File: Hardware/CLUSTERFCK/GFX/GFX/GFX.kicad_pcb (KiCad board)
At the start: 4 copper layers, 141.9 x 122.1 mm, 302 parts, among them J1 Conn_02x20_Counter_Clockwise, J2 Conn_02x20_Counter_Clockwise, U1 74LS08, U10 74LS08, U11 74HCT574, U12 74HCT574, U13 74LS08, U14 74LS08, U15 74LS08, U18 74HCT574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

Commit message: 0030 | 4,5h | Review GFX
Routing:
- net +5V: track 863.6 -> 747.8 mm
- net CLK: track 255.5 -> 242.3 mm
- net GFXCLK: track 146.4 -> 156.8 mm
- net Net-(D125-Pad2): track 170.6 -> 160.4 mm
- net Net-(D128-Pad2): track 140.5 -> 130.5 mm
- net Net-(D124-Pad2): track 181.0 -> 171.0 mm
- net Net-(D127-Pad2): track 150.8 -> 140.8 mm
- net Net-(D126-Pad2): track 160.5 -> 150.7 mm
- net Net-(D91-Pad2): track 115.9 -> 107.0 mm
- net GND: track 144.1 -> 135.4 mm, vias 89 -> 178
- net Net-(D77-Pad2): track 104.7 -> 97.0 mm
- net Net-(D78-Pad2): track 94.2 -> 86.9 mm
- net GFX3: track 113.3 -> 106.5 mm
- net Net-(D94-Pad2): track 107.0 -> 100.8 mm
- net Net-(D79-Pad2): track 83.3 -> 77.1 mm
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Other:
- board text added: "Leon Hellmich (Reviewed: Kevin da Silva Fernandes) 2020"
- board text removed: "Leon Hellmich 2020"

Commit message: unstable switching device push
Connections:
- J2 pad 10: Net-(J2-Pad10) -> GFX0
- J2 pad 12: Net-(J2-Pad12) -> GFX1
- J2 pad 13: Net-(J2-Pad13) -> GFX2
- J2 pad 14: Net-(J2-Pad14) -> GFX3
- J2 pad 15: Net-(J2-Pad15) -> GFXI
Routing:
- net GFXI: track 107.1 -> 243.8 mm, vias 2 -> 3
- net GFX3: track 106.5 -> 235.3 mm, vias 3 -> 6
- net GFX2: track 104.2 -> 231.0 mm, vias 3 -> 5
- net GFX1: track 100.0 -> 222.0 mm, vias 3 -> 6
- net GFX0: track 98.2 -> 219.0 mm, vias 3 -> 5

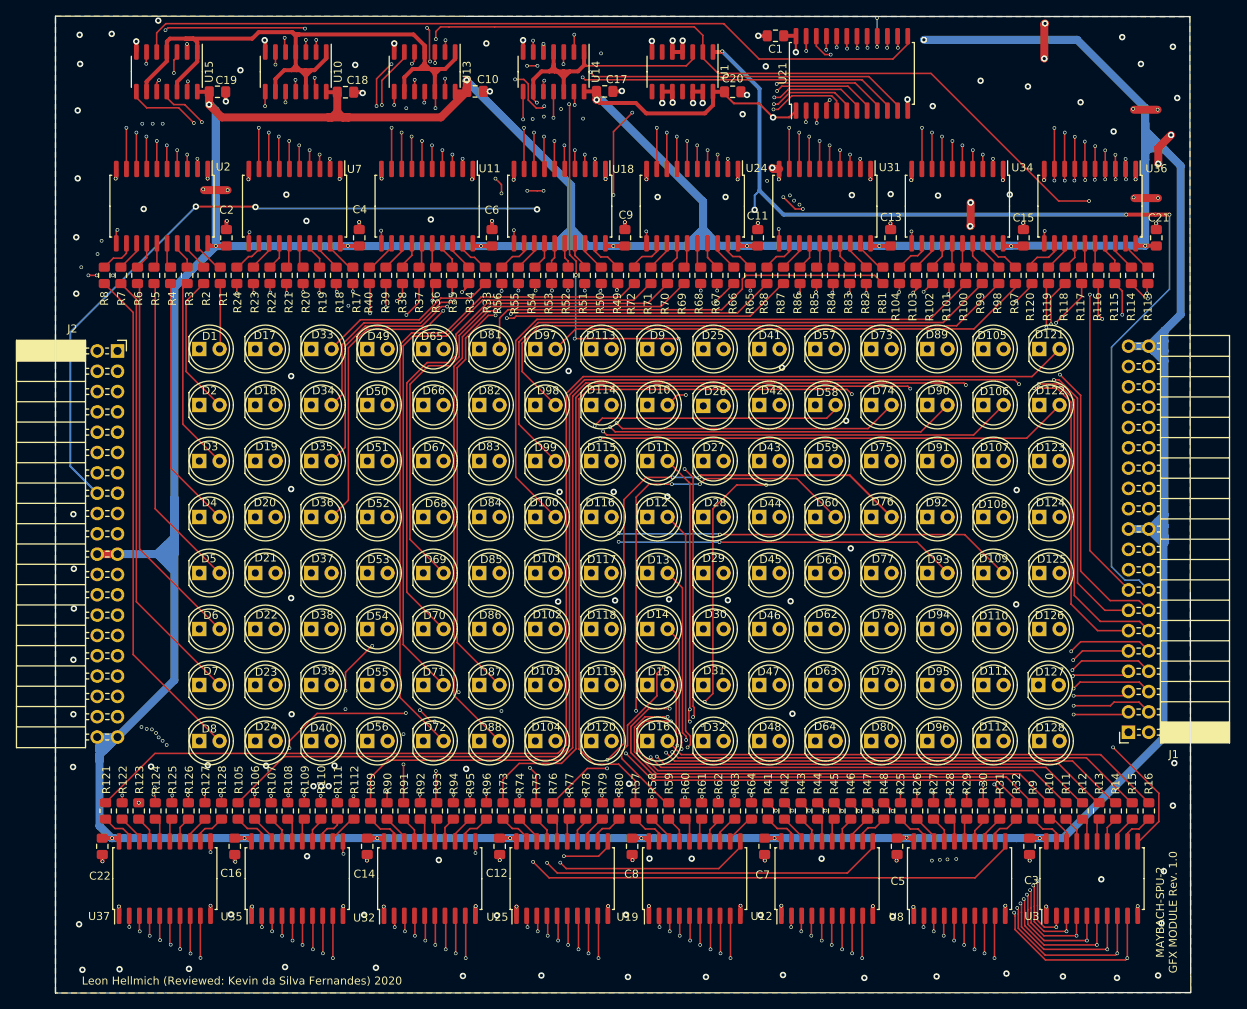
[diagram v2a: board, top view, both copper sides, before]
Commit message: 0032| 1 | Final cosmetics on GFX
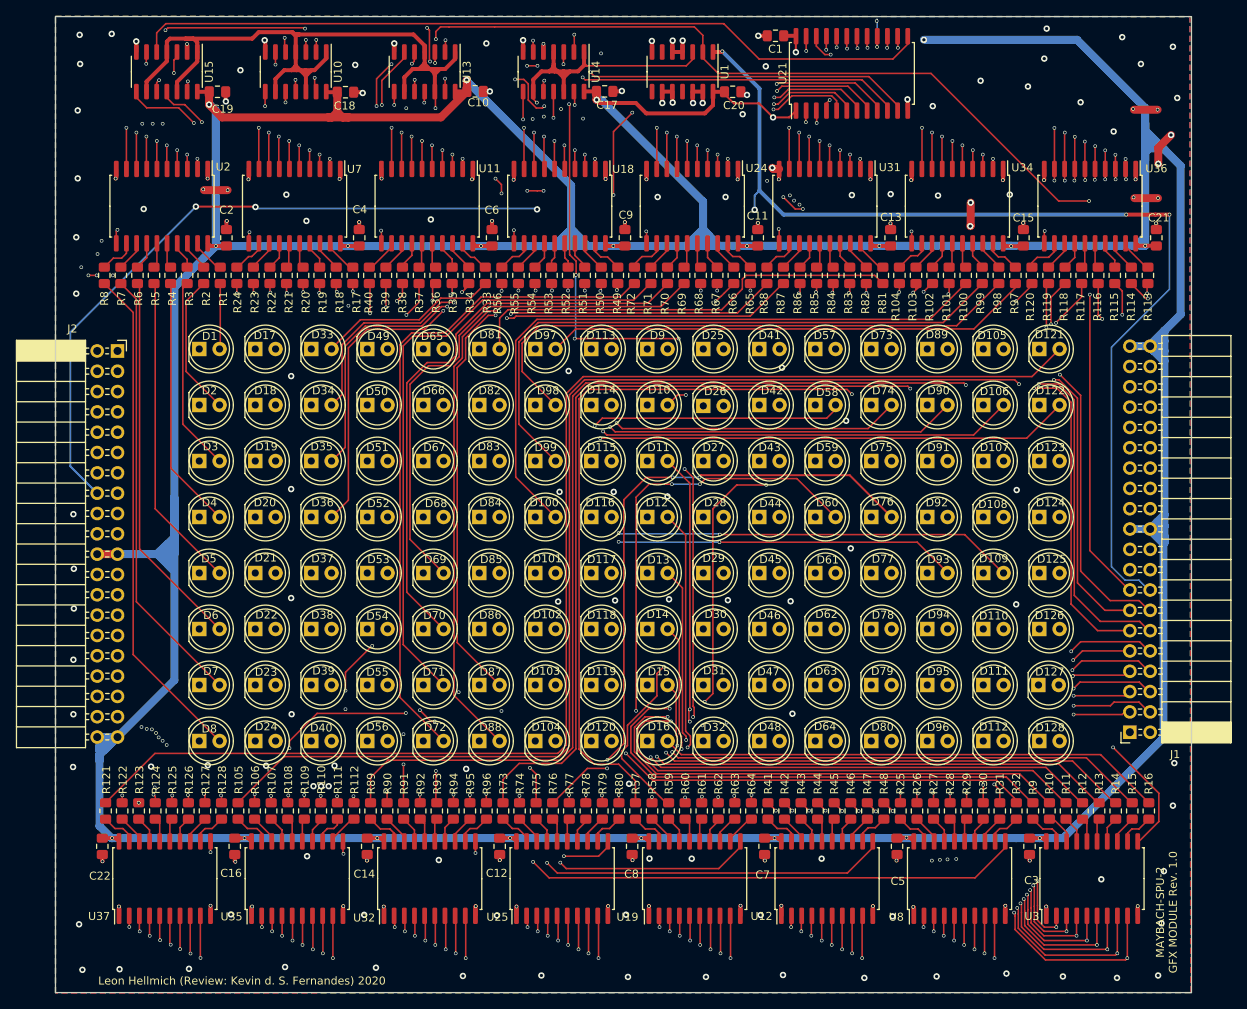
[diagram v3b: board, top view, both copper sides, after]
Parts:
- moved J1 0.17 mm to (167.7, 126.7)
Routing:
- net GND: track 135.4 -> 131.0 mm
- net (no net): vias 1 -> 0
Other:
- board size 141.9 x 122.1 mm -> 142 x 122 mm
- board text added: "Leon Hellmich (Review: Kevin d. S. Fernandes) 2020"
- board text removed: "Leon Hellmich (Reviewed: Kevin da Silva Fernandes) 2020"
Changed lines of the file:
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@@
     (thickness 1.64)
     (drawings 13)
-    (tracks 3886)
+    (tracks 3881)
     (modules 302)
     (nets 353)
@@
       (dielectric_constraints no)
     )
-    (last_trace_width 0.2)
+    (last_trace_width 0.25)
     (user_trace_width 0.2)
     (user_trace_width 0.25)
@@
   )
   (module "Connector_PinSocket_2.54mm:PinSocket_2x20_P2.54mm_Horizontal" (layer "F.Cu")
-    (at 167.475602 126.703674 180)
+    (at 167.65 126.703674 180)
     (descr "Through hole angled socket strip, 2x20, 2.54mm pitch, 8.51mm socket length, double cols (from Kicad 4.0.7), script generated")
     (tags "Through hole angled socket strip THT 2x20 2.54mm double row")
@@
     (tags "capacitor handsolder")
     (attr smd)
-    (fp_text reference "C20" (at 0 -1.65) (layer "F.SilkS")
+    (fp_text reference "C20" (at 0.15 1.7) (layer "F.SilkS")
       (effects (font (size 1 1) (thickness 0.15)))
     )
@@
     (tags "capacitor handsolder")
     (attr smd)
-    (fp_text reference "C19" (at 1.1 -1.45) (layer "F.SilkS")
+    (fp_text reference "C19" (at 0.65 2.15) (layer "F.SilkS")
       (effects (font (size 1 1) (thickness 0.15)))
     )
@@
     (tags "capacitor handsolder")
     (attr smd)
-    (fp_text reference "C18" (at 1.5 -1.5) (layer "F.SilkS")
+    (fp_text reference "C18" (at -0.1 1.7) (layer "F.SilkS")
       (effects (font (size 1 1) (thickness 0.15)))
     )
@@
     (tags "capacitor handsolder")
     (attr smd)
-    (fp_text reference "C17" (at 1.5 -1.5) (layer "F.SilkS")
+    (fp_text reference "C17" (at 0.3 1.7) (layer "F.SilkS")
       (effects (font (size 1 1) (thickness 0.15)))
     )
@@
     (tags "capacitor handsolder")
     (attr smd)
-    (fp_text reference "C10" (at 1.6 -1.5) (layer "F.SilkS")
+    (fp_text reference "C10" (at 0.4 1.4) (layer "F.SilkS")
       (effects (font (size 1 1) (thickness 0.15)))
     )
@@
   (gr_line (start 140.92 71.14) (end 140.92 71.34) (layer "F.Cu") (width 0.2))
   (gr_line (start 141.07 71.24) (end 140.91 71.09) (layer "F.Cu") (width 0.2))
-  (gr_line (start 33.35 159.3) (end 33.35 37.2) (layer "Edge.Cuts") (width 0.05))
-  (gr_line (start 175.25 159.25) (end 33.35 159.3) (layer "Edge.Cuts") (width 0.05))
-  (gr_line (start 175.15 37.25) (end 175.25 159.25) (layer "Edge.Cuts") (width 0.05))
-  (gr_line (start 33.35 37.2) (end 175.15 37.25) (layer "Edge.Cuts") (width 0.05))
-  (gr_text "Leon Hellmich (Reviewed: Kevin da Silva Fernandes) 2020\n" (at 56.66 157.78) (layer "F.SilkS")
+  (gr_line (start 33.35 159.25) (end 33.35 37.25) (layer "Edge.Cuts") (width 0.05))
+  (gr_line (start 175.35 159.25) (end 33.35 159.25) (layer "Edge.Cuts") (width 0.05))
+  (gr_line (start 175.35 37.25) (end 175.35 159.25) (layer "Edge.Cuts") (width 0.05))
+  (gr_line (start 33.35 37.25) (end 175.35 37.25) (layer "Edge.Cuts") (width 0.05))
+  (gr_text "Leon Hellmich (Review: Kevin d. S. Fernandes) 2020\n" (at 56.66 157.78) (layer "F.SilkS")
     (effects (font (size 1 1) (thickness 0.25)))
   )
@@
   (segment (start 138.615 48.335) (end 135.03001 44.75001) (width 0.2) (layer "F.Cu") (net 296))
   (segment (start 138.615 49) (end 138.615 48.335) (width 0.2) (layer "F.Cu") (net 296))
-  (segment (start 135.03001 44.75001) (end 100.75001 44.75001) (width 0.2) (layer "F.Cu") (net 296))
+  (segment (start 135.03 44.75) (end 100.75 44.75) (width 0.2) (layer "F.Cu") (net 296))
   (segment (start 100.75001 44.75001) (end 100.2 44.2) (width 0.2) (layer "F.Cu") (net 296))
   (segment (start 137.345 48.335) (end 134.16002 45.15002) (width 0.2) (layer "F.Cu") (net 321))
@@
   (segment (start 49.6 40) (end 57.95001 40) (width 0.5) (layer "F.Cu") (net 291))
   (segment (start 57.95001 40) (end 58.75 39.20001) (width 0.5) (layer "F.Cu") (net 291))
-  (via (at 46.2 37.75) (size 0.8) (drill 0.4) (layers "F.Cu" "B.Cu") (net 0))
   (segment (start 45.3 131) (end 35.6 131) (width 1) (layer "In2.Cu") (net 1))
   (segment (start 35.6 131) (end 35.55 131.05) (width 1) (layer "In2.Cu") (net 1))
@@
   (segment (start 123.093674 56.293674) (end 122.95 56.15) (width 1) (layer "F.Cu") (net 1))
   (via (at 119.25 49.45) (size 0.8) (drill 0.4) (layers "F.Cu" "B.Cu") (net 1))
-  (segment (start 156.95 42.5) (end 156.95 38.2) (width 1) (layer "F.Cu") (net 1))
-  (segment (start 156.95 38.2) (end 157.05 38.1) (width 1) (layer "F.Cu") (net 1))
   (segment (start 147.75 60.5) (end 147.75 63.4) (width 1) (layer "F.Cu") (net 1))
   (segment (start 147.75 63.4) (end 147.7 63.45) (width 1) (layer "F.Cu") (net 1))
   (via (at 147.75 60.5) (size 0.8) (drill 0.4) (layers "F.Cu" "B.Cu") (net 1))
   (via (at 147.7 63.45) (size 0.8) (drill 0.4) (layers "F.Cu" "B.Cu") (net 1))
-  (via (at 157.05 38.1) (size 0.8) (drill 0.4) (layers "F.Cu" "B.Cu") (net 1))
+  (via (at 157.25 38.75) (size 0.8) (drill 0.4) (layers "F.Cu" "B.Cu") (net 1))
   (via (at 156.95 42.5) (size 0.8) (drill 0.4) (layers "F.Cu" "B.Cu") (net 1))
   (segment (start 171.2 55.65) (end 171.2 53.65) (width 1) (layer "F.Cu") (net 1))
@@
   (via (at 136.05 41.05) (size 0.45) (drill 0.3) (layers "F.Cu" "B.Cu") (net 318))
   (segment (start 136.075 41.025) (end 136.05 41.05) (width 0.2) (layer "F.Cu") (net 318))
-  (segment (start 136.05 37.42501) (end 136.04999 37.425) (width 0.2) (layer "B.Cu") (net 318))
-  (segment (start 136.05 41.05) (end 136.05 37.42501) (width 0.2) (layer "B.Cu") (net 318))
+  (segment (start 136.05 41.17499) (end 136.05 37.55) (width 0.2) (layer "B.Cu") (net 318))
   (segment (start 46.3 45.2) (end 46.3 41.6) (width 0.2) (layer "In1.Cu") (net 318))
   (segment (start 50.35001 37.54999) (end 136.04999 37.54999) (width 0.2) (layer "In1.Cu") (net 318))
-  (segment (start 136.04999 37.54999) (end 136.04999 37.425) (width 0.2) (layer "In1.Cu") (net 318))
-  (via (at 136.04999 37.425) (size 0.45) (drill 0.3) (layers "F.Cu" "B.Cu") (net 318))
+  (via (at 136 37.8) (size 0.45) (drill 0.3) (layers "F.Cu" "B.Cu") (net 318))
   (segment (start 46 46.625) (end 46 45.5) (width 0.2) (layer "F.Cu") (net 318))
   (via (at 46.3 45.2) (size 0.45) (drill 0.3) (layers "F.Cu" "B.Cu") (net 318))
